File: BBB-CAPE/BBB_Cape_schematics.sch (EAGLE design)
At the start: 81 parts, among them IC1 EEPROM-I2CSMD, SW2 219-02

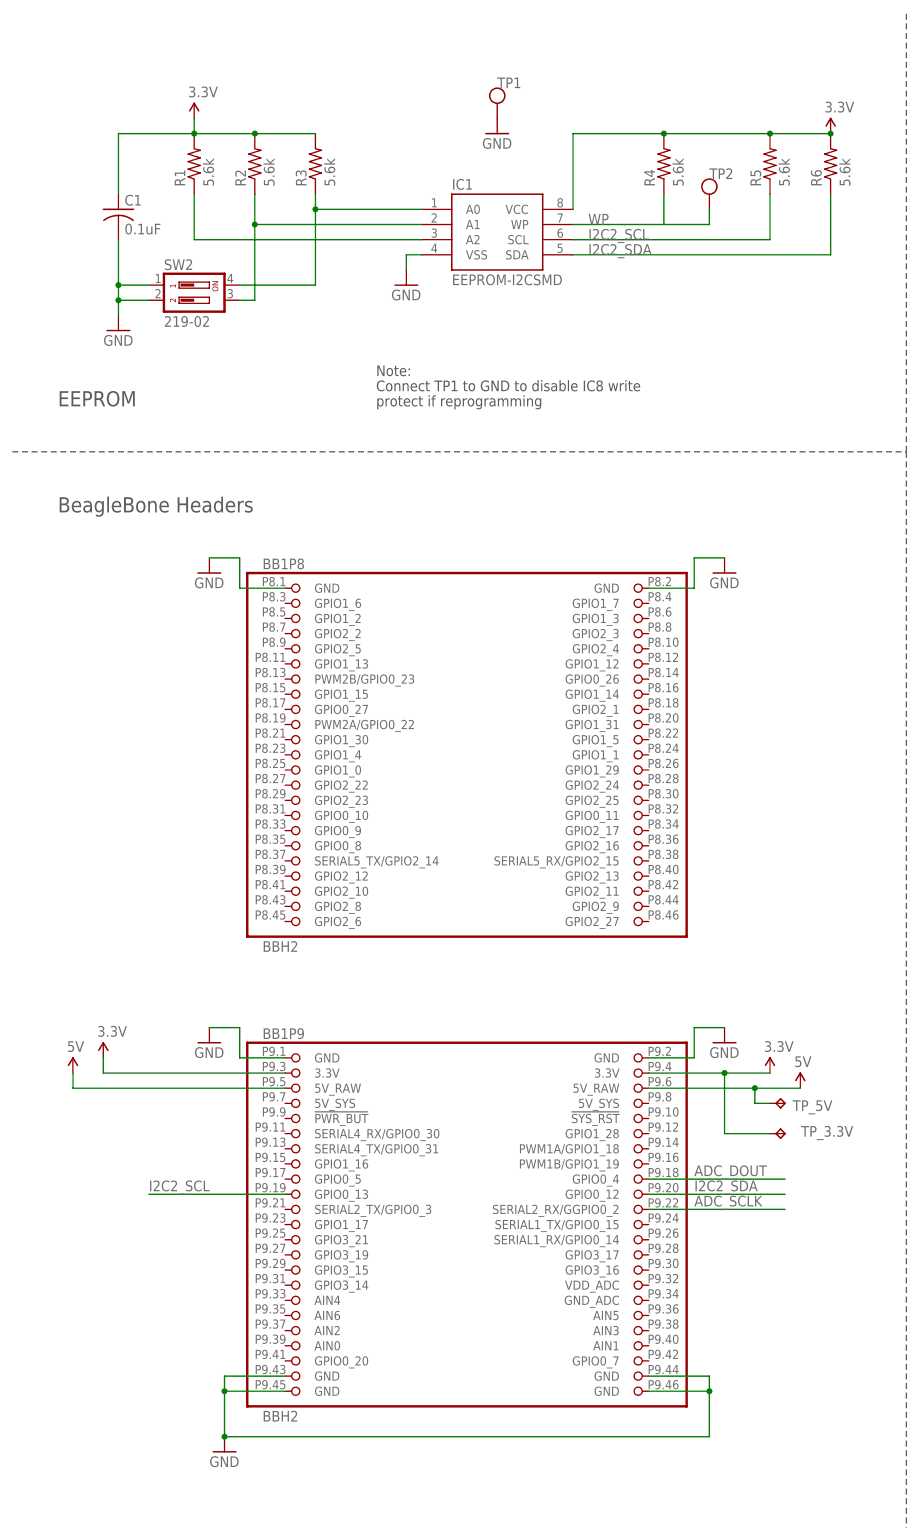
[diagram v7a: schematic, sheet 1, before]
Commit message: Add signal label and remove warnings by ERC (Electric Rule Check) in BBB_Cape_schematics.sch
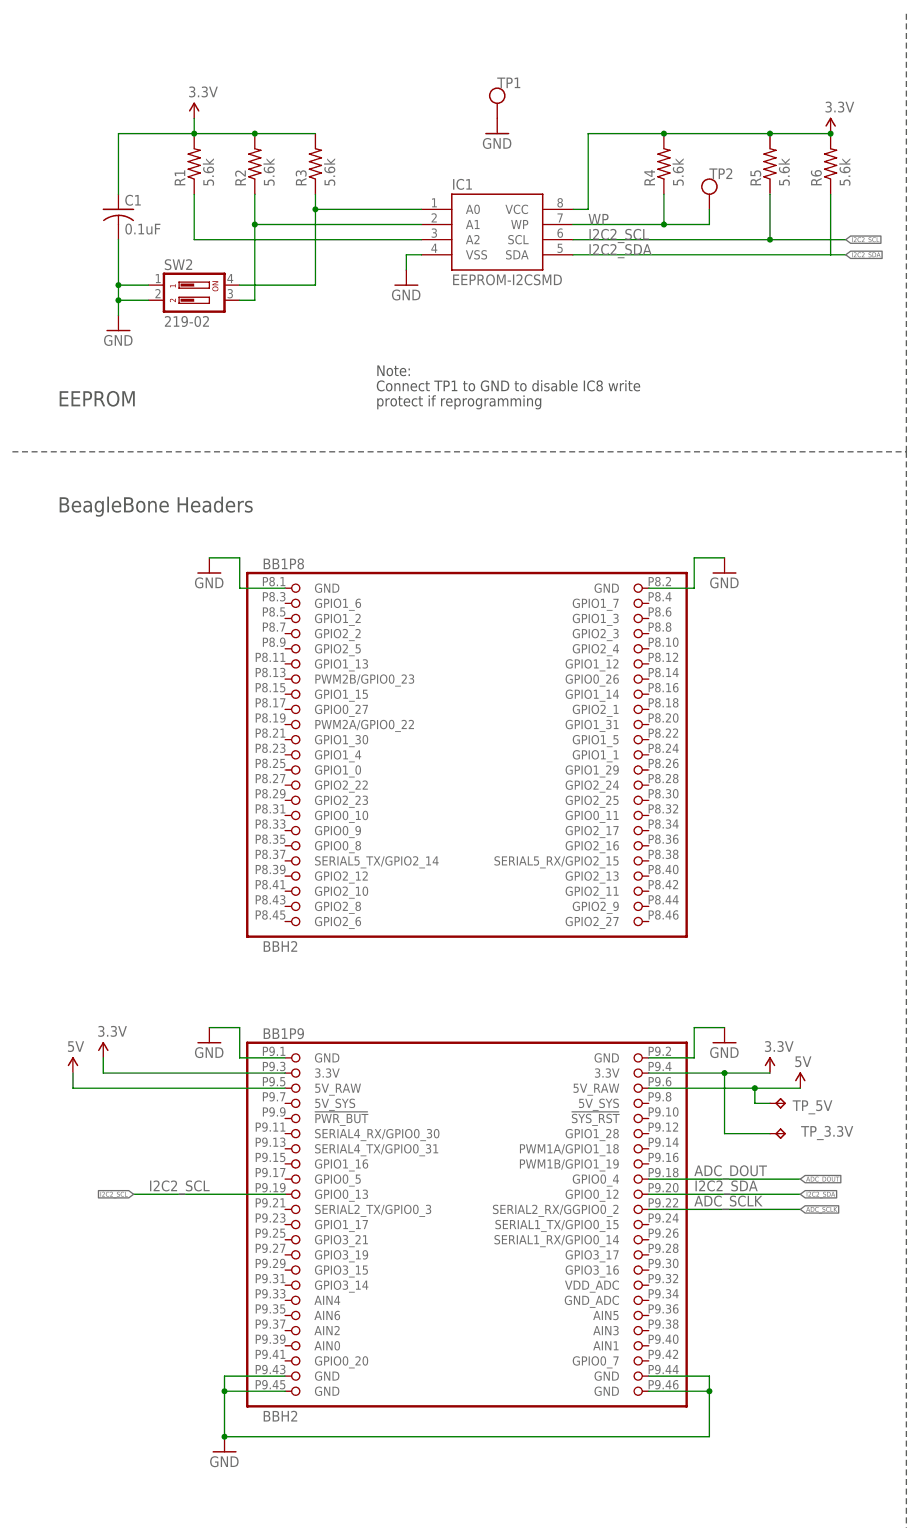
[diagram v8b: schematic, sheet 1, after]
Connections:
- net N$20 renamed ECG_LPF
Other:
- moved on the sheet: TP_ECG_LPF
